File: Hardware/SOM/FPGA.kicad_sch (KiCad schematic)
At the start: 83 parts, among them U1 LFE5UM5G-85F

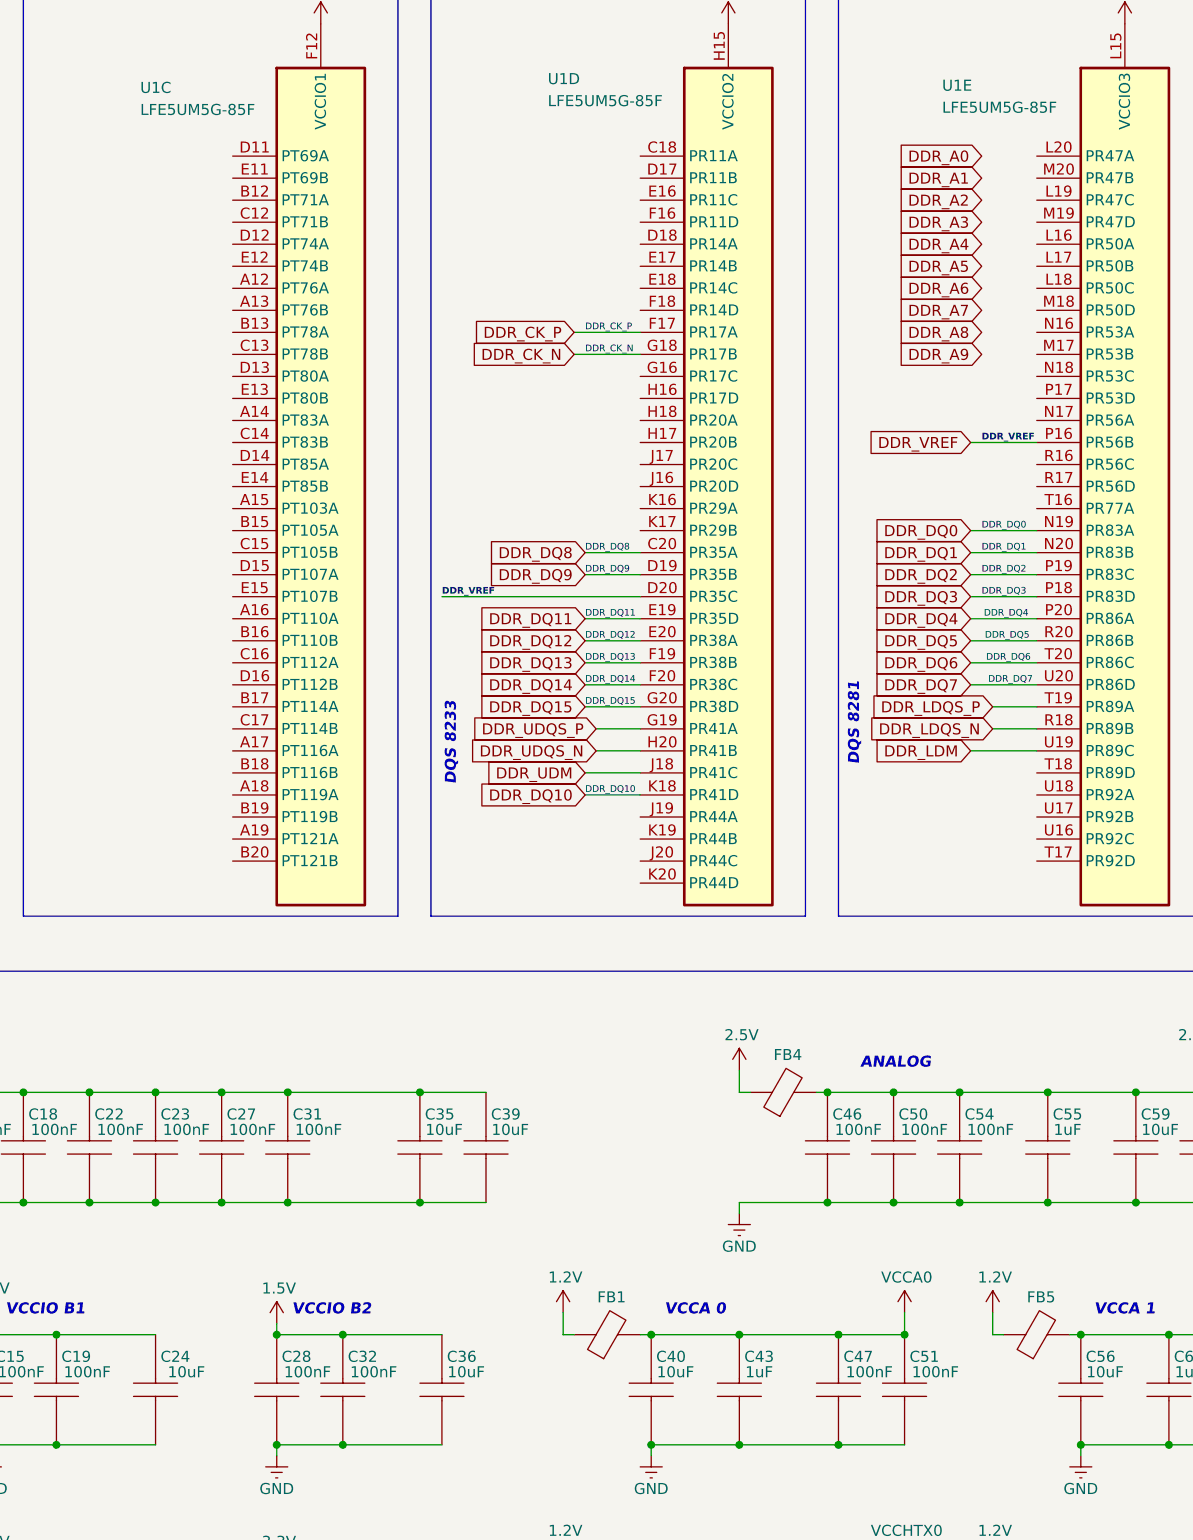
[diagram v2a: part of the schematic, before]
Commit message: SOM: decoupling caps placement
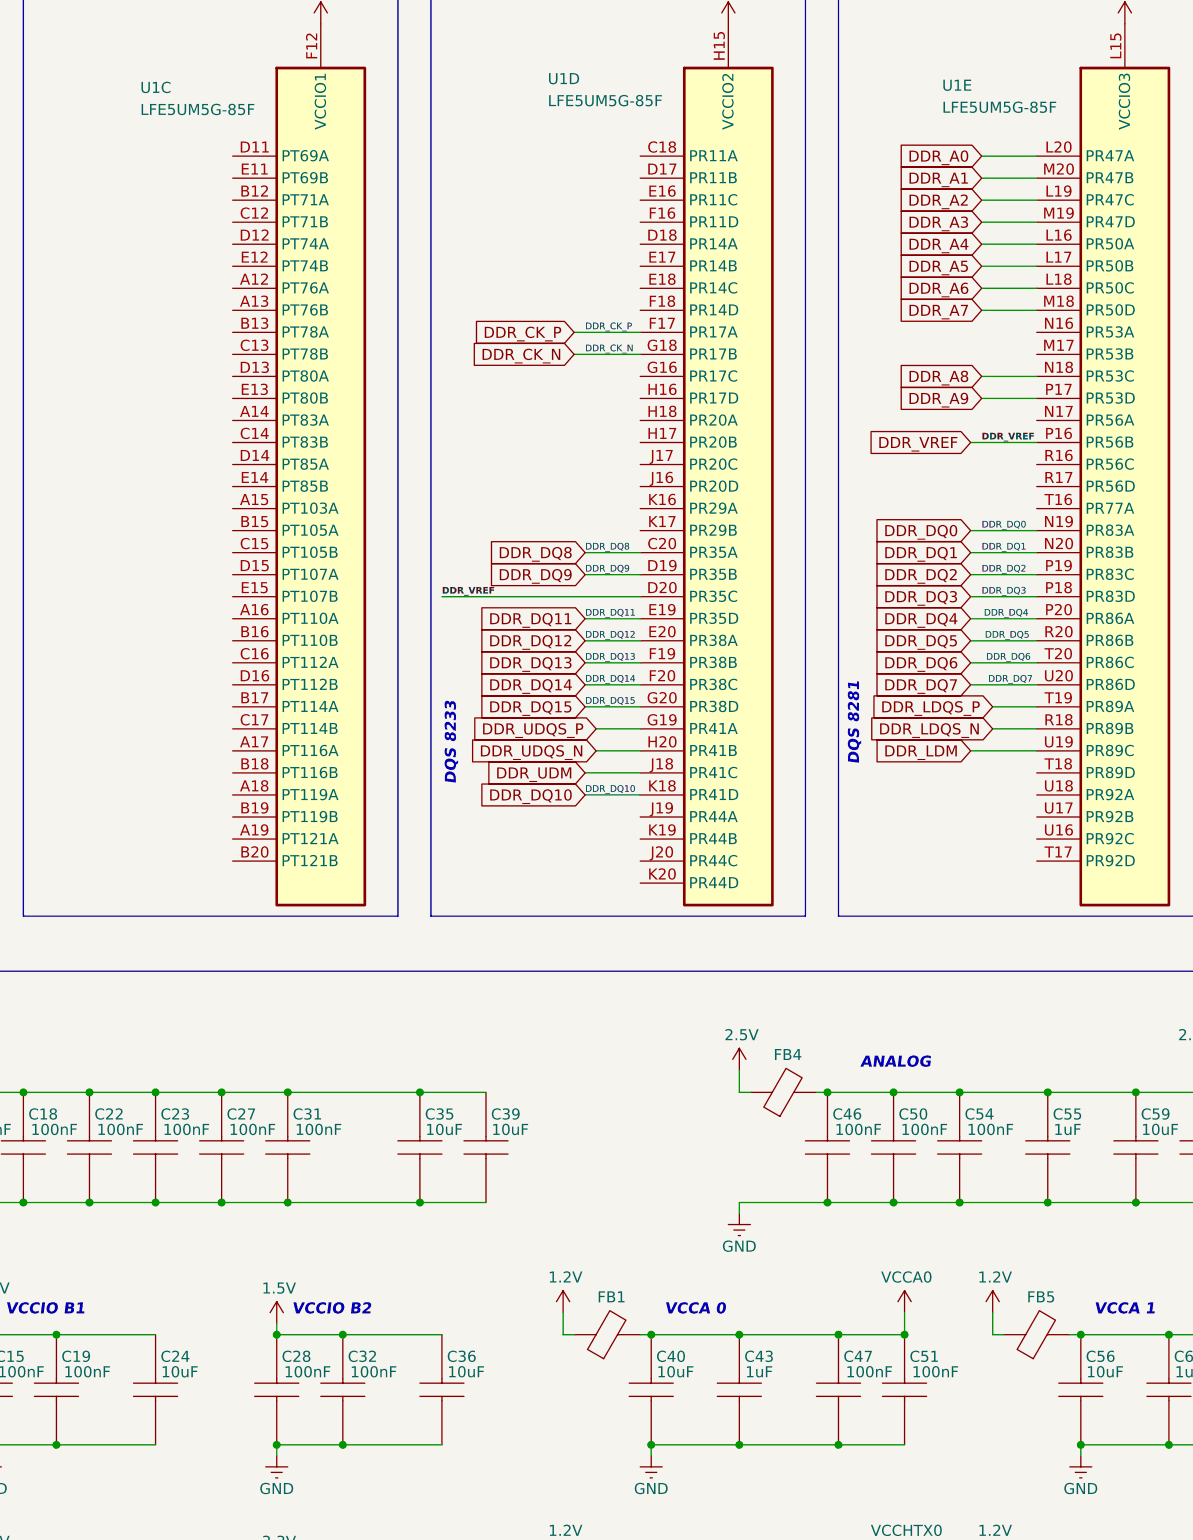
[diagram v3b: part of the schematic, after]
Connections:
- net DDR_A0: now also U1.L20 (PR47A)
- net DDR_A1: now also U1.M20 (PR47B)
- net DDR_A2: now also U1.L19 (PR47C)
- net DDR_A3: now also U1.M19 (PR47D)
- net DDR_A4: now also U1.L16 (PR50A)
- net DDR_A5: now also U1.L17 (PR50B)
- net DDR_A6: now also U1.L18 (PR50C)
- net DDR_A7: now also U1.M18 (PR50D)
- net DDR_A8: now also U1.N18 (PR53C)
- net DDR_A9: now also U1.P17 (PR53D)
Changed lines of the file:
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@@
 	(wire
 		(pts
+			(xy 173.99 71.12) (xy 180.34 71.12)
+		)
+		(stroke
+			(width 0)
+			(type default)
+		)
+	)
+	(wire
+		(pts
 			(xy 154.94 151.13) (xy 156.21 151.13)
 		)
@@
 	(wire
 		(pts
+			(xy 173.99 45.72) (xy 180.34 45.72)
+		)
+		(stroke
+			(width 0)
+			(type default)
+		)
+	)
+	(wire
+		(pts
 			(xy 185.42 191.77) (xy 185.42 193.04)
 		)
@@
 	(wire
 		(pts
+			(xy 173.99 43.18) (xy 180.34 43.18)
+		)
+		(stroke
+			(width 0)
+			(type default)
+		)
+	)
+	(wire
+		(pts
 			(xy 125.73 208.28) (xy 127 208.28)
 		)
@@
 	(wire
 		(pts
+			(xy 173.99 50.8) (xy 180.34 50.8)
+		)
+		(stroke
+			(width 0)
+			(type default)
+		)
+	)
+	(wire
+		(pts
 			(xy 214.63 205.74) (xy 214.63 208.28)
 		)
@@
 	(wire
 		(pts
+			(xy 173.99 55.88) (xy 180.34 55.88)
+		)
+		(stroke
+			(width 0)
+			(type default)
+		)
+	)
+	(wire
+		(pts
 			(xy 92.71 220.98) (xy 100.33 220.98)
 		)
@@
 	(wire
 		(pts
+			(xy 173.99 58.42) (xy 180.34 58.42)
+		)
+		(stroke
+			(width 0)
+			(type default)
+		)
+	)
+	(wire
+		(pts
 			(xy 34.29 250.19) (xy 45.72 250.19)
 		)
@@
 	(wire
 		(pts
+			(xy 173.99 53.34) (xy 180.34 53.34)
+		)
+		(stroke
+			(width 0)
+			(type default)
+		)
+	)
+	(wire
+		(pts
 			(xy 134.62 179.07) (xy 135.89 179.07)
 		)
@@
 	(wire
 		(pts
+			(xy 173.99 60.96) (xy 180.34 60.96)
+		)
+		(stroke
+			(width 0)
+			(type default)
+		)
+	)
+	(wire
+		(pts
 			(xy 146.05 220.98) (xy 157.48 220.98)
 		)
@@
 	(wire
 		(pts
+			(xy 173.99 68.58) (xy 180.34 68.58)
+		)
+		(stroke
+			(width 0)
+			(type default)
+		)
+	)
+	(wire
+		(pts
 			(xy 92.71 179.07) (xy 92.71 177.8)
 		)
@@
 	(wire
 		(pts
+			(xy 173.99 48.26) (xy 180.34 48.26)
+		)
+		(stroke
+			(width 0)
+			(type default)
+		)
+	)
+	(wire
+		(pts
 			(xy 175.26 106.68) (xy 180.34 106.68)
 		)
@@
 	(global_label "DDR_A9"
 		(shape input)
-		(at 173.99 66.04 180)
+		(at 173.99 71.12 180)
 		(fields_autoplaced yes)
 		(effects
@@
 		)
 		(property "Intersheetrefs" "${INTERSHEET_REFS}"
-			(at 163.9291 66.04 0)
+			(at 163.9291 71.12 0)
 			(effects
 				(font
@@
 	(global_label "DDR_A8"
 		(shape input)
-		(at 173.99 63.5 180)
+		(at 173.99 68.58 180)
 		(fields_autoplaced yes)
 		(effects
@@
 		)
 		(property "Intersheetrefs" "${INTERSHEET_REFS}"
-			(at 163.9291 63.5 0)
+			(at 163.9291 68.58 0)
 			(effects
 				(font
@@
 		)
 		(property "Value" "10uF"
-			(at 82.296 183.388 90)
+			(at 81.534 183.388 90)
 			(effects
 				(font

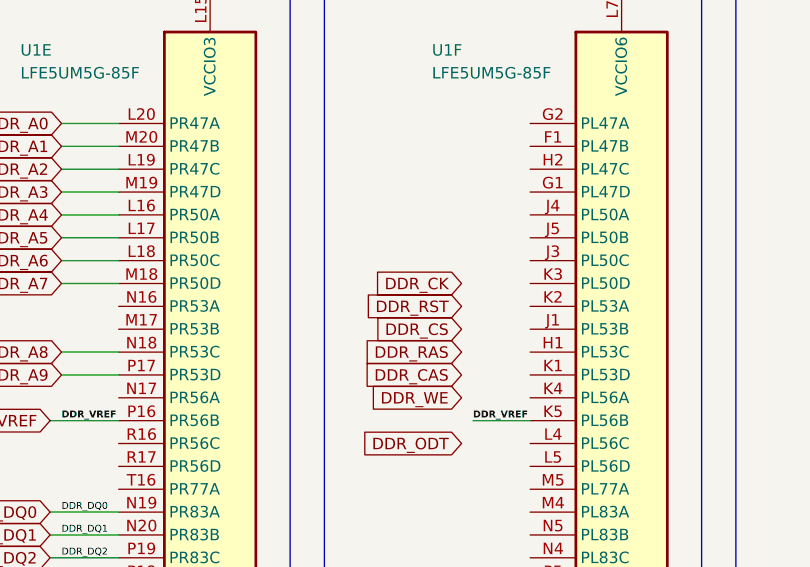
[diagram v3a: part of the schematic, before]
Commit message: DDR clock schematics fixed
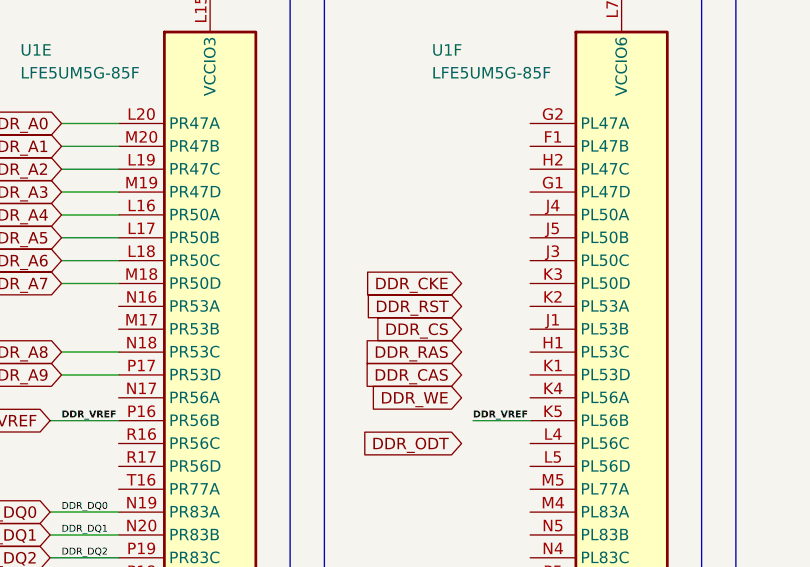
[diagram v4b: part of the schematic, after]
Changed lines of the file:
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@@
 		)
 	)
-	(global_label "DDR_CK"
+	(global_label "DDR_CKE"
 		(shape input)
 		(at 218.44 60.96 180)
@@
 		)
 		(property "Intersheetrefs" "${INTERSHEET_REFS}"
-			(at 208.1372 60.96 0)
+			(at 206.9882 60.96 0)
 			(effects
 				(font

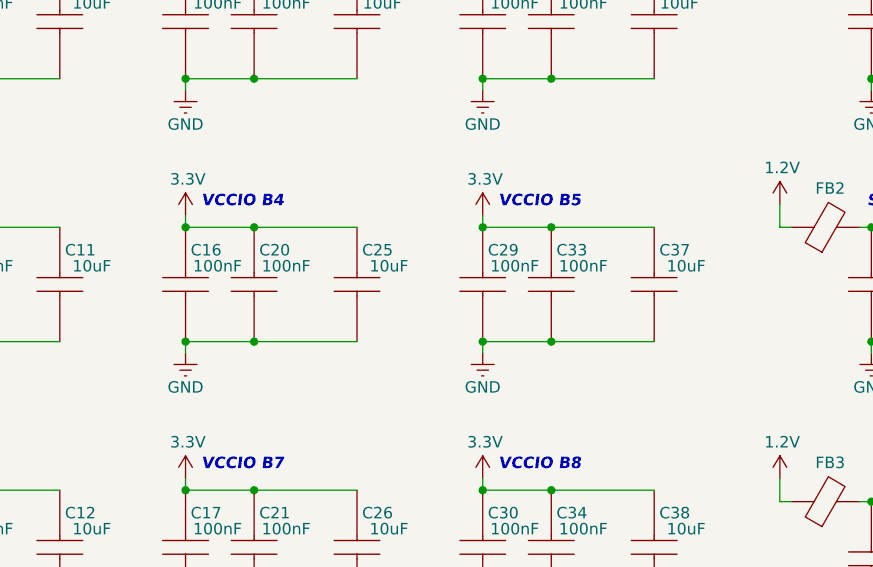
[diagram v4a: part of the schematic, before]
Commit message: SOM: decoupling caps placement
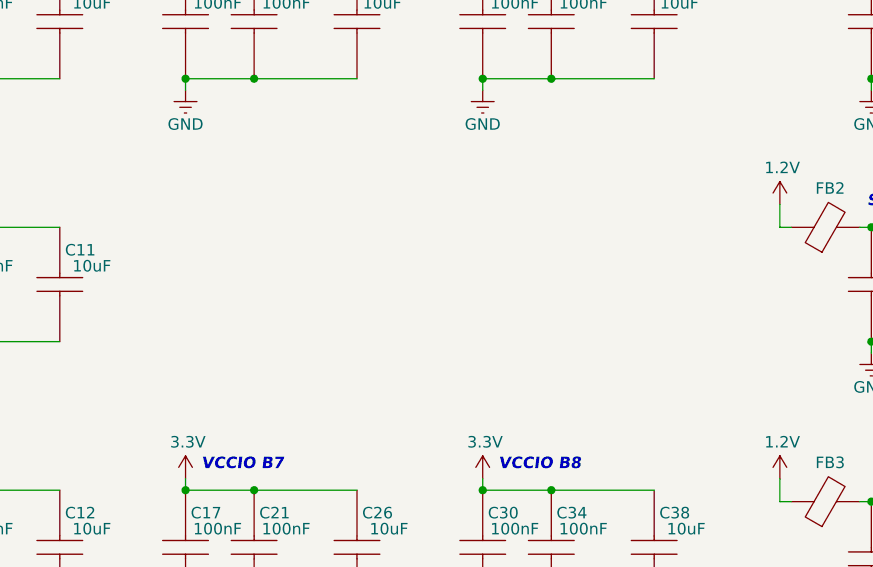
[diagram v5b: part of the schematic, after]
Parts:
- removed C16, C20, C29, C33: 100nF, Capacitor_SMD:C_0402_1005Metric, symbol RA8M1:885012205092
- removed C25, C37: 10uF, Capacitor_SMD:C_0402_1005Metric, symbol RA8M1:885012205092
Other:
- note removed: "VCCIO B4"
- note removed: "VCCIO B5"

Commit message: DDR reconnect
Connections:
- net DDR_A10: now also U1.C18 (PR11A)
- net DDR_A11: now also U1.D17 (PR11B)
- net DDR_A12: now also U1.E16 (PR11C)
- net DDR_A13: now also U1.F16 (PR11D)
- net DDR_A14: now also U1.D18 (PR14A)
- net DDR_BA0: now also U1.E17 (PR14B)
- net DDR_BA1: now also U1.E18 (PR14C)
- net DDR_BA2: now also U1.F18 (PR14D)
- net DDR_CAS: now also U1.J17 (PR20C)
- net DDR_CKE: now also U1.G16 (PR17C)
- net DDR_CS: now also U1.H18 (PR20A)
- net DDR_ODT: now also U1.K16 (PR29A)
- net DDR_RAS: now also U1.H17 (PR20B)
- net DDR_RST: now also U1.H16 (PR17D)
- net DDR_WE: now also U1.J16 (PR20D)
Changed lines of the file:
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@@
 	(wire
 		(pts
+			(xy 127 48.26) (xy 134.62 48.26)
+		)
+		(stroke
+			(width 0)
+			(type default)
+		)
+	)
+	(wire
+		(pts
 			(xy 165.1 179.07) (xy 157.48 179.07)
 		)
@@
 	(wire
 		(pts
+			(xy 127 73.66) (xy 134.62 73.66)
+		)
+		(stroke
+			(width 0)
+			(type default)
+		)
+	)
+	(wire
+		(pts
 			(xy 134.62 238.76) (xy 135.89 238.76)
 		)
@@
 	(wire
 		(pts
+			(xy 127 83.82) (xy 134.62 83.82)
+		)
+		(stroke
+			(width 0)
+			(type default)
+		)
+	)
+	(wire
+		(pts
 			(xy 195.58 191.77) (xy 207.01 191.77)
 		)
@@
 	(wire
 		(pts
+			(xy 127 53.34) (xy 134.62 53.34)
+		)
+		(stroke
+			(width 0)
+			(type default)
+		)
+	)
+	(wire
+		(pts
 			(xy 219.71 76.2) (xy 226.06 76.2)
 		)
@@
 	(wire
 		(pts
+			(xy 127 71.12) (xy 134.62 71.12)
+		)
+		(stroke
+			(width 0)
+			(type default)
+		)
+	)
+	(wire
+		(pts
 			(xy 173.99 43.18) (xy 180.34 43.18)
 		)
@@
 	(wire
 		(pts
+			(xy 127 81.28) (xy 134.62 81.28)
+		)
+		(stroke
+			(width 0)
+			(type default)
+		)
+	)
+	(wire
+		(pts
 			(xy 34.29 191.77) (xy 45.72 191.77)
 		)
@@
 	(wire
 		(pts
+			(xy 127 43.18) (xy 134.62 43.18)
+		)
+		(stroke
+			(width 0)
+			(type default)
+		)
+	)
+	(wire
+		(pts
 			(xy 184.15 208.28) (xy 185.42 208.28)
 		)
@@
 	(wire
 		(pts
+			(xy 127 45.72) (xy 134.62 45.72)
+		)
+		(stroke
+			(width 0)
+			(type default)
+		)
+	)
+	(wire
+		(pts
 			(xy 234.95 162.56) (xy 246.38 162.56)
 		)
@@
 	(wire
 		(pts
+			(xy 127 78.74) (xy 134.62 78.74)
+		)
+		(stroke
+			(width 0)
+			(type default)
+		)
+	)
+	(wire
+		(pts
 			(xy 63.5 151.13) (xy 71.12 151.13)
 		)
@@
 	(wire
 		(pts
+			(xy 127 76.2) (xy 134.62 76.2)
+		)
+		(stroke
+			(width 0)
+			(type default)
+		)
+	)
+	(wire
+		(pts
 			(xy 34.29 250.19) (xy 45.72 250.19)
 		)
@@
 	(wire
 		(pts
+			(xy 127 60.96) (xy 134.62 60.96)
+		)
+		(stroke
+			(width 0)
+			(type default)
+		)
+	)
+	(wire
+		(pts
 			(xy 165.1 208.28) (xy 157.48 208.28)
 		)
@@
 	(wire
 		(pts
+			(xy 127 50.8) (xy 134.62 50.8)
+		)
+		(stroke
+			(width 0)
+			(type default)
+		)
+	)
+	(wire
+		(pts
 			(xy 314.96 73.66) (xy 317.5 73.66)
 		)
@@
 	(wire
 		(pts
+			(xy 127 68.58) (xy 134.62 68.58)
+		)
+		(stroke
+			(width 0)
+			(type default)
+		)
+	)
+	(wire
+		(pts
+			(xy 127 58.42) (xy 134.62 58.42)
+		)
+		(stroke
+			(width 0)
+			(type default)
+		)
+	)
+	(wire
+		(pts
 			(xy 241.3 223.52) (xy 241.3 233.68)
 		)
@@
 	(wire
 		(pts
+			(xy 127 55.88) (xy 134.62 55.88)
+		)
+		(stroke
+			(width 0)
+			(type default)
+		)
+	)
+	(wire
+		(pts
 			(xy 165.1 236.22) (xy 165.1 238.76)
 		)
@@
 	(global_label "DDR_A13"
 		(shape input)
-		(at 218.44 114.3 180)
+		(at 127 50.8 180)
 		(fields_autoplaced yes)
 		(effects
@@
 		)
 		(property "Intersheetrefs" "${INTERSHEET_REFS}"
-			(at 207.1696 114.3 0)
+			(at 115.7296 50.8 0)
 			(effects
 				(font
@@
 	(global_label "DDR_WE"
 		(shape input)
-		(at 218.44 73.66 180)
+		(at 127 81.28 180)
 		(fields_autoplaced yes)
 		(effects
@@
 		)
 		(property "Intersheetrefs" "${INTERSHEET_REFS}"
-			(at 208.0768 73.66 0)
+			(at 116.6368 81.28 0)
 			(effects
 				(font
@@
 	(global_label "DDR_A11"
 		(shape input)
-		(at 218.44 109.22 180)
+		(at 127 45.72 180)
 		(fields_autoplaced yes)
 		(effects
@@
 		)
 		(property "Intersheetrefs" "${INTERSHEET_REFS}"
-			(at 207.1696 109.22 0)
+			(at 115.7296 45.72 0)
 			(effects
 				(font
@@
 	(global_label "DDR_BA2"
 		(shape input)
-		(at 218.44 124.46 180)
+		(at 127 60.96 180)
 		(fields_autoplaced yes)
 		(effects
@@
 		)
 		(property "Intersheetrefs" "${INTERSHEET_REFS}"
-			(at 207.1091 124.46 0)
+			(at 115.6691 60.96 0)
 			(effects
 				(font
@@
 	(global_label "DDR_CAS"
 		(shape input)
-		(at 218.44 71.12 180)
+		(at 127 78.74 180)
 		(fields_autoplaced yes)
 		(effects
@@
 		)
 		(property "Intersheetrefs" "${INTERSHEET_REFS}"
-			(at 207.1091 71.12 0)
+			(at 115.6691 78.74 0)
 			(effects
 				(font
@@
 	(global_label "DDR_A10"
 		(shape input)
-		(at 218.44 106.68 180)
+		(at 127 43.18 180)
 		(fields_autoplaced yes)
 		(effects
@@
 		)
 		(property "Intersheetrefs" "${INTERSHEET_REFS}"
-			(at 207.1696 106.68 0)
+			(at 115.7296 43.18 0)
 			(effects
 				(font
@@
 	(global_label "DDR_A12"
 		(shape input)
-		(at 218.44 111.76 180)
+		(at 127 48.26 180)
 		(fields_autoplaced yes)
 		(effects
@@
 		)
 		(property "Intersheetrefs" "${INTERSHEET_REFS}"
-			(at 207.1696 111.76 0)
+			(at 115.7296 48.26 0)
 			(effects
 				(font
@@
 	(global_label "DDR_RAS"
 		(shape input)
-		(at 218.44 68.58 180)
+		(at 127 76.2 180)
 		(fields_autoplaced yes)
 		(effects
@@
 		)
 		(property "Intersheetrefs" "${INTERSHEET_REFS}"
-			(at 207.1091 68.58 0)
+			(at 115.6691 76.2 0)
 			(effects
 				(font
@@
 	(global_label "DDR_RST"
 		(shape input)
-		(at 218.44 63.5 180)
+		(at 127 71.12 180)
 		(fields_autoplaced yes)
 		(effects
@@
 		)
 		(property "Intersheetrefs" "${INTERSHEET_REFS}"
-			(at 207.2301 63.5 0)
+			(at 115.7901 71.12 0)
 			(effects
 				(font
@@
 	(global_label "DDR_A14"
 		(shape input)
-		(at 218.44 116.84 180)
+		(at 127 53.34 180)
 		(fields_autoplaced yes)
 		(effects
@@
 		)
 		(property "Intersheetrefs" "${INTERSHEET_REFS}"
-			(at 207.1696 116.84 0)
+			(at 115.7296 53.34 0)
 			(effects
 				(font
@@
 	(global_label "DDR_BA0"
 		(shape input)
-		(at 218.44 119.38 180)
+		(at 127 55.88 180)
 		(fields_autoplaced yes)
 		(effects
@@
 		)
 		(property "Intersheetrefs" "${INTERSHEET_REFS}"
-			(at 207.1091 119.38 0)
+			(at 115.6691 55.88 0)
 			(effects
 				(font
@@
 	(global_label "DDR_ODT"
 		(shape input)
-		(at 218.44 78.74 180)
+		(at 127 83.82 180)
 		(fields_autoplaced yes)
 		(effects
@@
 		)
 		(property "Intersheetrefs" "${INTERSHEET_REFS}"
-			(at 207.1091 78.74 0)
+			(at 115.6691 83.82 0)
 			(effects
 				(font
@@
 	(global_label "DDR_BA1"
 		(shape input)
-		(at 218.44 121.92 180)
+		(at 127 58.42 180)
 		(fields_autoplaced yes)
 		(effects
@@
 		)
 		(property "Intersheetrefs" "${INTERSHEET_REFS}"
-			(at 207.1091 121.92 0)
+			(at 115.6691 58.42 0)
 			(effects
 				(font
@@
 	(global_label "DDR_CS"
 		(shape input)
-		(at 218.44 66.04 180)
+		(at 127 73.66 180)
 		(fields_autoplaced yes)
 		(effects
@@
 		)
 		(property "Intersheetrefs" "${INTERSHEET_REFS}"
-			(at 208.1977 66.04 0)
+			(at 116.7577 73.66 0)
 			(effects
 				(font
@@
 	(global_label "DDR_CKE"
 		(shape input)
-		(at 218.44 60.96 180)
+		(at 127 68.58 180)
 		(fields_autoplaced yes)
 		(effects
@@
 		)
 		(property "Intersheetrefs" "${INTERSHEET_REFS}"
-			(at 206.9882 60.96 0)
+			(at 115.5482 68.58 0)
 			(effects
 				(font
@@
 		(dnp no)
 		(property "Reference" "U1"
-			(at 123.952 34.29 0)
+			(at 123.952 34.544 0)
 			(effects
 				(font
